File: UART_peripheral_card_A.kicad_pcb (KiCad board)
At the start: 2 copper layers, 94.5 x 54 mm, 61 parts, among them J1 PP1_edgeConnnector_TE_5-55308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, J2 power_connector, J3 UART_connector, J4 OUTPUT_MODE, U1 74AHC1G32, U10 74AHC1G08, U11 74AHC1G32, U12 74AHC1G04, U13 74AHC595, U14 74HCT107, U15 CD74AC161M, U16 LTC6990CS6, U17 LTC6994xS6-1, U18 74AHC1G32, U19 74AHC1G32, U2 74AHC1G32, U20 74AHC1G08, U21 74AHC1G32, U22 74AHC1G04, U23 74AHC1G04, U24 74AHC1G08, U25 74AHC1G32, U26 74HC165, U27 74AHC1G126, U28 74AHC1G126, U3 74AHC1G04, U4 74AHC1G32, U5 74AHC1G32, U6 LTC6994xS6-1, U7 LTC6990CS6, U8 CD74AC161M, U9 74HCT107

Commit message: Finish pcb routing
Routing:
- net GND: track 441.6 -> 144.0 mm, vias 12 -> 15
- net +5V: track 310.8 -> 317.8 mm
- net /Transmission/ZERO: track 108.2 -> 111.2 mm
- net /~CS_MODULE: track 59.3 -> 62.2 mm
- net VCC: track 117.0 -> 118.3 mm
- net /Transmission/TX_DATA: track 48.4 -> 49.7 mm
- net /Reception/~RECEIVING_STAT: track 18.5 -> 19.5 mm
- net /Reception/RECEIVING_STAT: track 70.4 -> 71.3 mm
- net /BREAD2_0: track 11.5 -> 12.2 mm
- net /~CLK_MODULE: track 27.9 -> 28.5 mm
- net /Transmission/Qa: track 21.5 -> 22.1 mm
- net /BREAD1_3: track 58.0 -> 58.5 mm
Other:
- rule pad_to_mask_clearance: 0.2 -> 0
- board text added: "1"
- board text added: "3.3V+"
- board text added: "5V+"
- board text added: "BOT"
- board text added: "GG"
- board text added: "GND"
- board text added: "Licensed under CERN-OHL-W v2 or later"
- board text added: "PP1"
- board text added: "RX"
- board text added: "TOP"
- board text added: "TX"
- board text added: "UART_peripheral_card - A V1.0"
- board text added: "VCC"
- board text removed: "PP1_PCB"

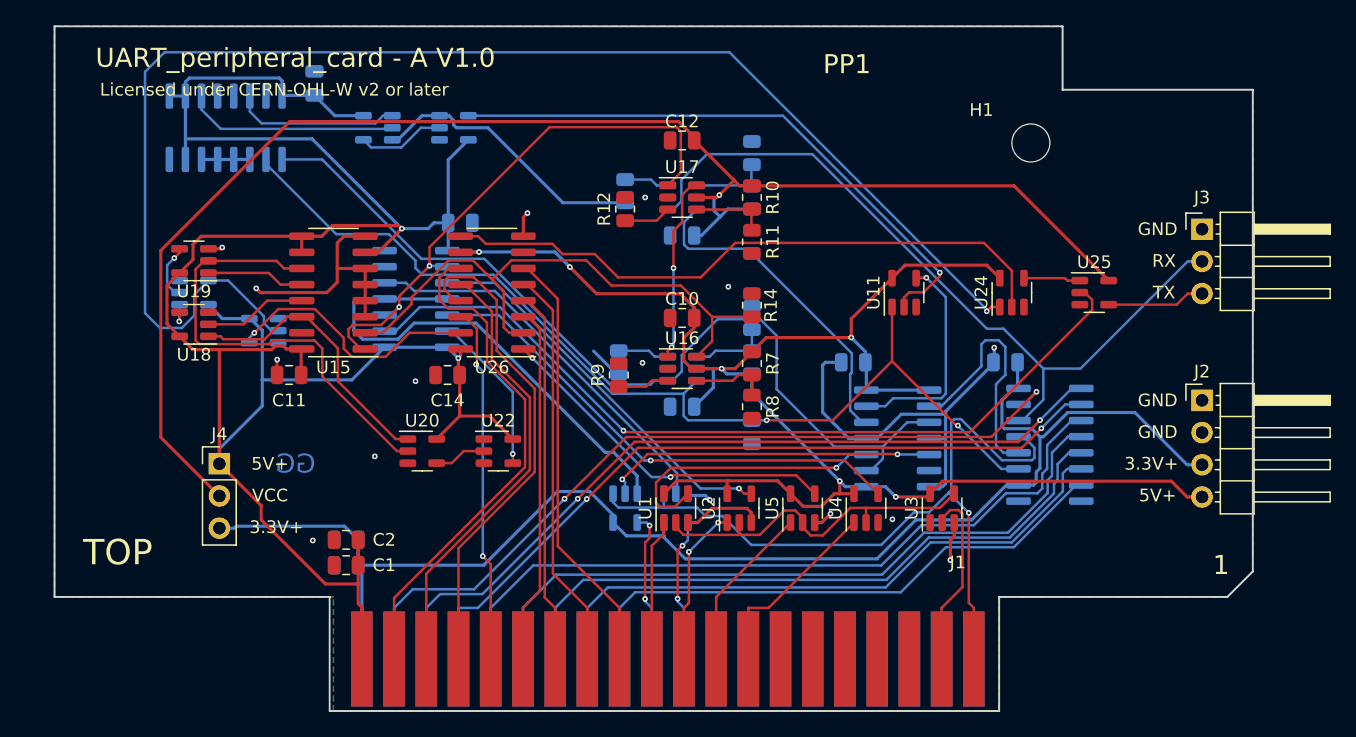
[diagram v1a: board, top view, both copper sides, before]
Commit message: Modify trackWidth,via diameter, first PCB 1.1 pass
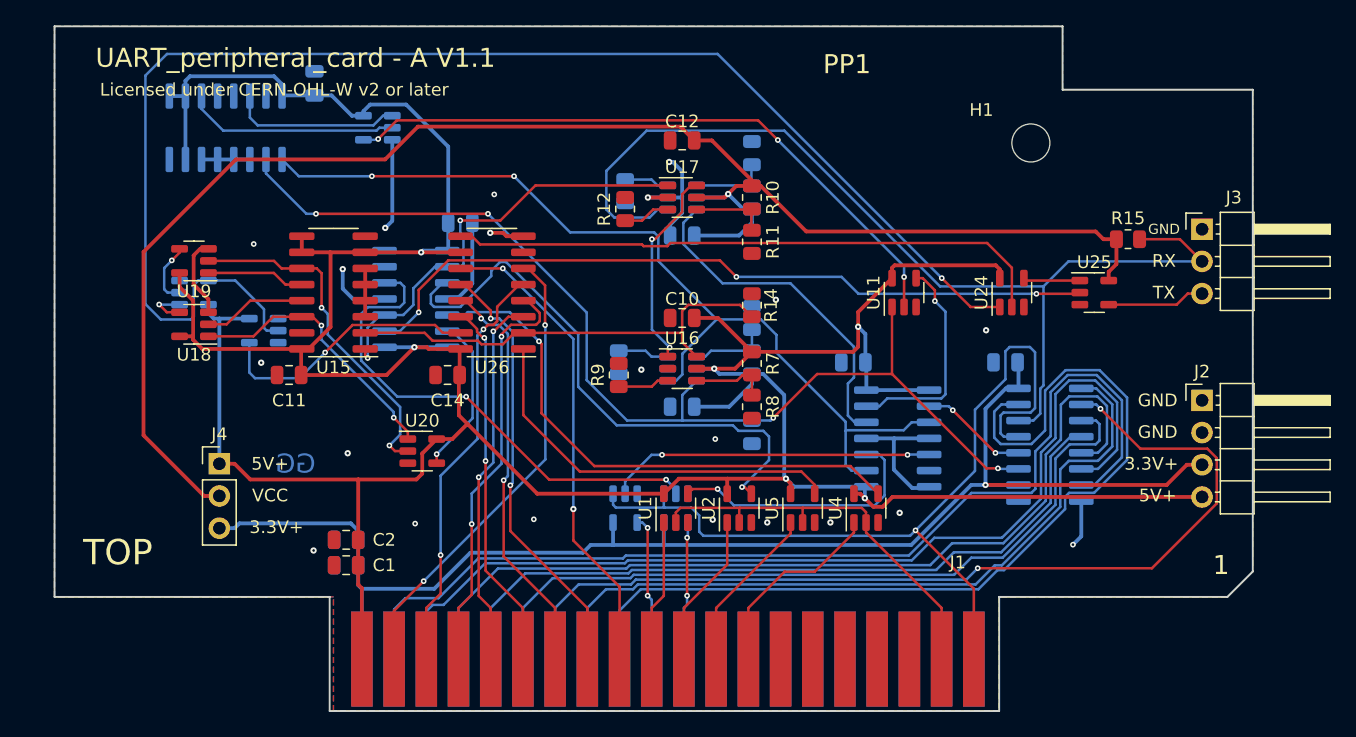
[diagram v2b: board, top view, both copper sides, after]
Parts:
- removed U12, U22, U3: 74AHC1G04, Package_TO_SOT_SMD:SOT-23-5
- added R15: 10k, Resistor_SMD:R_0805_2012Metric, F.Cu at (168.2, 83.8)
- U1, U2, U4, U5: value 74AHC1G32 -> 74AHC1G00
- U10, U20: value 74AHC1G08 -> 74AHC1G00
- U27, U28: value 74AHC1G126 -> 74AHC1G125
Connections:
- U1 pad 2: /~CLK_MODULE -> /CLK_MODULE
- U10 pad 4: /Reception/STOP_CONDITION -> /Reception/~STOP_CONDITION
- U13 pad 1: /BREAD1_1 -> /BREAD1_6
- U13 pad 15: /BREAD1_0 -> /BREAD1_7
- U13 pad 2: /BREAD1_2 -> /BREAD1_5
- U13 pad 3: /BREAD1_3 -> /BREAD1_4
- U13 pad 4: /BREAD1_4 -> /BREAD1_3
- U13 pad 5: /BREAD1_5 -> /BREAD1_2
- U13 pad 6: /BREAD1_6 -> /BREAD1_1
- U13 pad 7: /BREAD1_7 -> /BREAD1_0
- U2 pad 2: /~CLK_MODULE -> /CLK_MODULE
- U20 pad 4: Net-(U20-Pad4) -> /Transmission/~INTERNAL_RESET
- U26 pad 11: /BWRITE1_0 -> /BWRITE1_7
- U26 pad 12: /BWRITE1_1 -> /BWRITE1_6
- U26 pad 13: /BWRITE1_2 -> /BWRITE1_5
- U26 pad 14: /BWRITE1_3 -> /BWRITE1_4
- U26 pad 3: /BWRITE1_4 -> /BWRITE1_3
- U26 pad 4: /BWRITE1_5 -> /BWRITE1_2
- U26 pad 5: /BWRITE1_6 -> /BWRITE1_1
- U26 pad 6: /BWRITE1_7 -> /BWRITE1_0
- U4 pad 2: /~CLK_MODULE -> /CLK_MODULE
- U5 pad 2: /~CLK_MODULE -> /CLK_MODULE
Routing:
- net GND: track 144.0 -> 68.0 mm, vias 15 -> 21
- net /BREAD1_7: track 44.5 -> 74.3 mm
- net /~CLK_MODULE: track 28.5 -> 0.00 mm
- net /BREAD1_5: track 51.8 -> 75.6 mm, vias 0 -> 2
- net +5V: track 317.8 -> 295.0 mm, vias 8 -> 6
- net /PERIPHERAL_RX: track 60.5 -> 80.3 mm
- net /CLK_MODULE: track 14.5 -> 33.3 mm
- net /BREAD1_0: track 63.6 -> 82.2 mm, vias 2 -> 0
- net /BREAD1_1: track 62.9 -> 77.9 mm, vias 2 -> 0
- net /~RST_TX_FLAG: track 30.9 -> 44.8 mm
- net /BREAD1_2: track 59.8 -> 71.4 mm, vias 2 -> 0
- net /Reception/~RECEIVING_STAT: track 19.5 -> 8.58 mm, vias 0 -> 2
- net /BREAD1_6: track 48.4 -> 58.7 mm
- net /Transmission/9600_BAUD: track 45.8 -> 35.9 mm
- net /Transmission/TRANSMITING_STAT: track 44.1 -> 34.6 mm
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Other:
- net class Power: trace_width 0.25 -> 0.3; via_dia 0.45 -> 0.5
- board text added: "UART_peripheral_card - A V1.1"
- board text removed: "UART_peripheral_card - A V1.0"
